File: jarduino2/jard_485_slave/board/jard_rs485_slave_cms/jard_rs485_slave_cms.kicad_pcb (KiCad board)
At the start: 2 copper layers, 94 x 94 mm, 56 parts, among them J1 NETWORK IN, J10 Conn_01x02, J2 NETWORK OUT, J3 LED, J4 Conn_01x03, J5 Conn_01x02, J6 Conn_01x03, J7 Conn_01x03, J8 Conn_01x02, J9 Conn_01x02, Q1 MMBT5550L, Q2 MMBT5550L, Q3 bpc_mos_p03p4, Q4 bpc_mos_p03p4, U1 LT1785AxN8, U2 AD8603, U3 AD8603

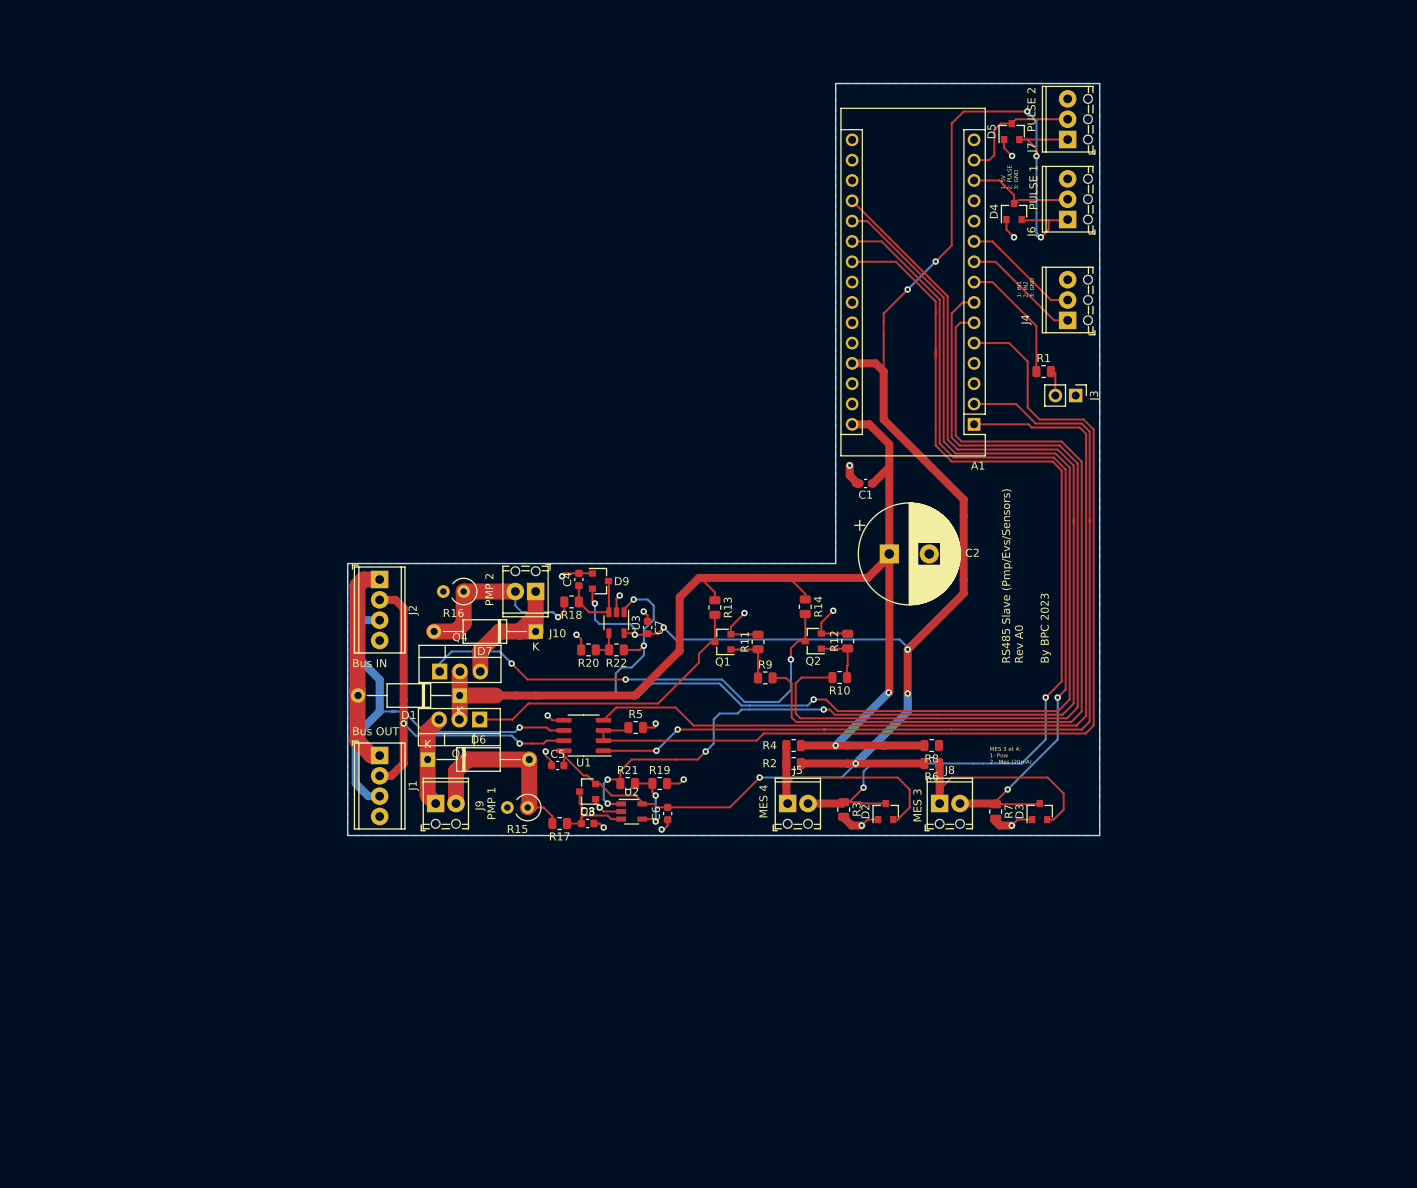
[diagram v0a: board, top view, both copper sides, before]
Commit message: Agrandir sérigraphie connecteurs bus Correction erreur inversion sérigraphie 1 et 4 sur J2 Correction inversion RX/TX sur module RS485 Inversion sérigraphie Niveaux/Débit
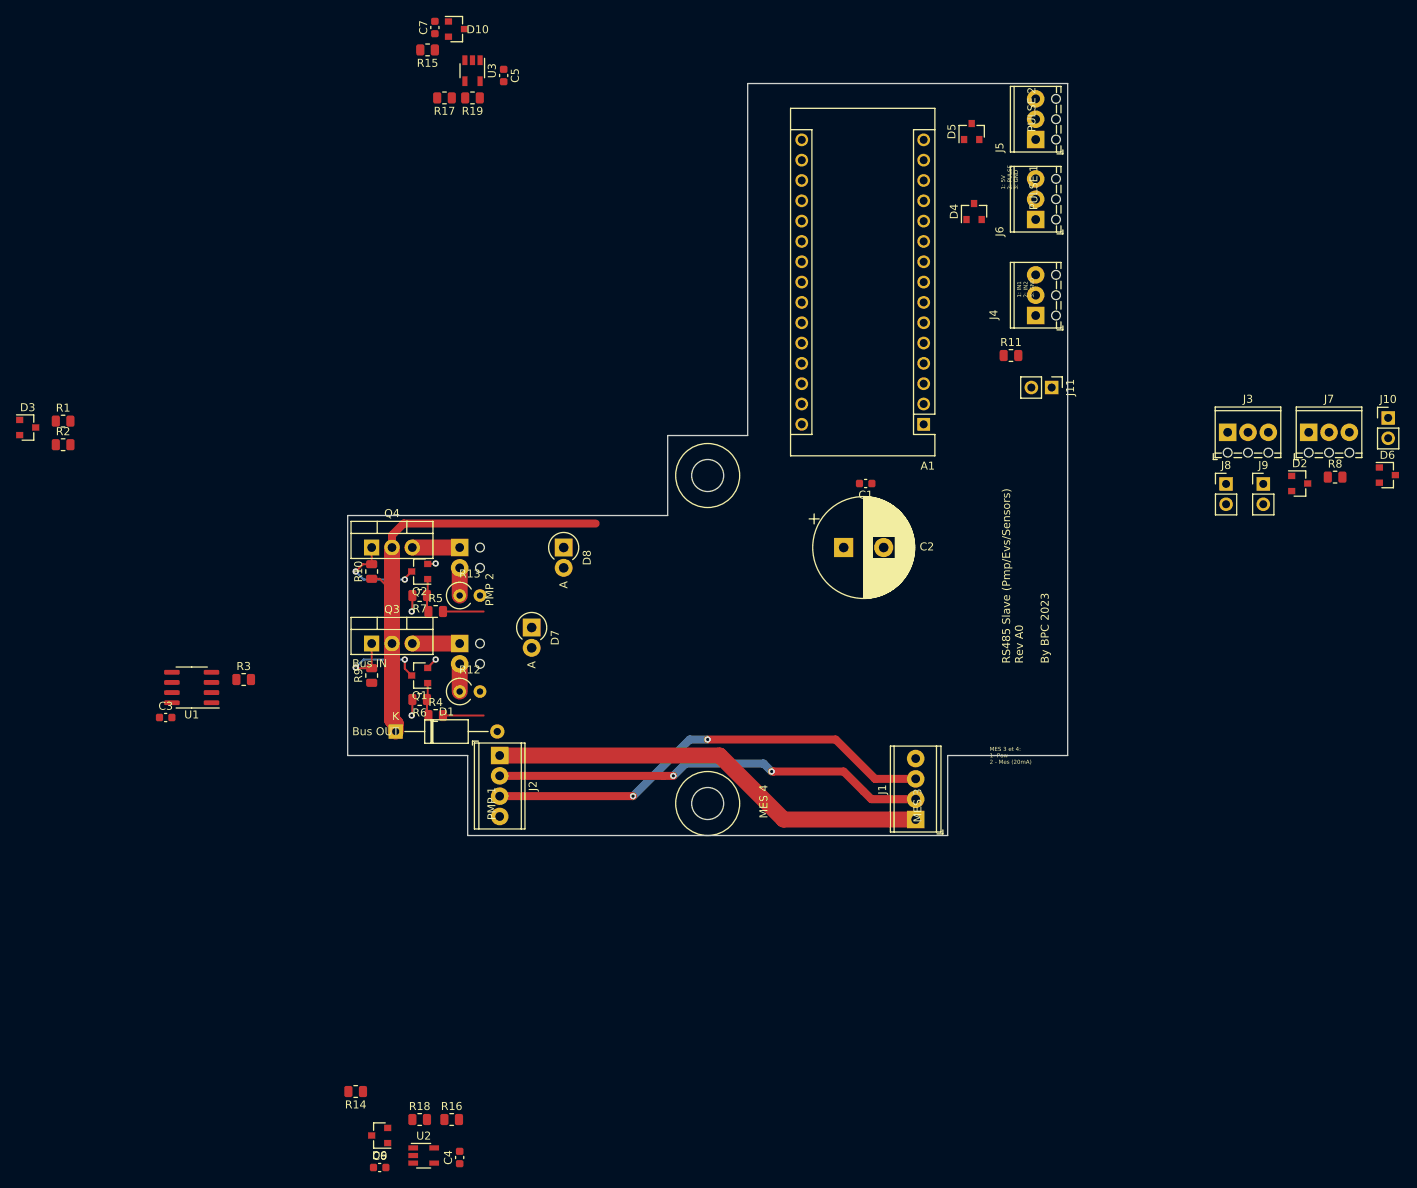
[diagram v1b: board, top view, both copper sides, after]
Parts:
- removed the D7 at (103.5, 114.5)
- removed the J5 at (135.0, 136.0)
- removed the R12 at (142.5, 115.7)
- removed the R3 at (142.0, 136.8)
- removed the R4 at (135.8, 128.8)
- removed the R6 at (153.0, 131.0)
- added D6: BAV99, Package_TO_SOT_SMD:SOT-23, F.Cu at (210.0, 95.0)
- added D8: D, Diode_THT:D_DO-15_P2.54mm_Vertical_AnodeUp, F.Cu at (107.0, 104.0)
- added J10: LED 1, Connector_PinHeader_2.54mm:PinHeader_1x02_P2.54mm_Vertical, F.Cu at (210.1, 87.8)
- added J3: Conn_01x03, TerminalBlock_Phoenix:TerminalBlock_Phoenix_MPT-0,5-3-2.54_1x03_P2.54mm_Horizontal, F.Cu at (190.0, 89.6)
- added J7: Conn_01x03, TerminalBlock_Phoenix:TerminalBlock_Phoenix_MPT-0,5-3-2.54_1x03_P2.54mm_Horizontal, F.Cu at (200.1, 89.6)
- added J9: BTN 2, Connector_PinHeader_2.54mm:PinHeader_1x02_P2.54mm_Vertical, F.Cu at (194.4, 96.0)
- added R1: 100k, Resistor_SMD:R_0805_2012Metric, F.Cu at (44.4, 88.2)
- added REF**: BPC_Trou4mm_Fixation, bpc:BPC_Trou4mm_Fixation, F.Cu at (125.0, 136.0)
- added REF**: BPC_Trou4mm_Fixation, bpc:BPC_Trou4mm_Fixation, F.Cu at (125.0, 95.0)
- D7: renamed from D6; footprint Diode_THT:D_A-405_P12.70mm_Horizontal -> Diode_THT:D_DO-15_P2.54mm_Vertical_AnodeUp
- J11: renamed from J3; value LED -> LED 2
- J12: renamed from J9; moved to B.Cu
- J13: renamed from J10; moved to B.Cu
- J8: value Conn_01x02 -> BTN 1; footprint TerminalBlock_Phoenix:TerminalBlock_Phoenix_MPT-0,5-2-2.54_1x02_P2.54mm_Horizontal -> Connector_PinHeader_2.54mm:PinHeader_1x02_P2.54mm_Vertical
- R2: value 0 -> 40k
- R7: value 250 -> 100k
- R8: value 0 -> 150
- moved D3 135.3 mm to (40.0, 89.0), turned to 0 degrees
- moved R2 99.6 mm to (44.4, 91.2)
- moved R7 76.9 mm to (89.0, 110.0), turned to 180 degrees
- moved C5 71.3 mm to (99.5, 45.0)
- moved C7 71.3 mm to (90.9, 39.0)
- moved D10 71.3 mm to (93.6, 39.2)
- moved R15 71.3 mm to (90.0, 41.8)
- moved R17 71.3 mm to (92.1, 47.8)
- moved R19 71.3 mm to (95.6, 47.8)
- moved U3 71.3 mm to (95.6, 44.4)
- moved J1 67.5 mm to (151.0, 138.0), turned to 90 degrees
- moved D2 66.0 mm to (199.0, 96.0), turned to 0 degrees
- moved R8 60.6 mm to (203.4, 95.2), turned to 0 degrees
- moved R10 54.4 mm to (83.0, 107.0), turned to 90 degrees
- moved J8 53.6 mm to (189.8, 96.0)
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- renumbered C5 to C3, C6 to C4, C7 to C5, C3 to C6, C4 to C7, D9 to D10, D8 to D9, J7 to J5, R14 to R10, R1 to R11, R15 to R12, R16 to R13, R17 to R14, R18 to R15, R19 to R16, R20 to R17, R21 to R18, R22 to R19, R5 to R3, R9 to R4, R10 to R5, R11 to R6, R13 to R9
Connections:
- A1 pad 10: IN_2 -> LED1
- A1 pad 11: Net-(A1-Pad11) -> LED2
- A1 pad 12: Net-(A1-Pad12) -> IN_1
- A1 pad 13: IN_PULSE_1 -> IN_2
- A1 pad 14: IN_PULSE_2 -> CMD_P1
- A1 pad 15: Net-(A1-Pad15) -> CMD_P2
- A1 pad 24: Net-(A1-Pad24) -> MES_POW
- A1 pad 25: Net-(A1-Pad25) -> BTN1
- A1 pad 26: Net-(A1-Pad26) -> BTN2
- A1 pad 5: TXEN -> IN_PULSE_1
- A1 pad 6: CMD_P1 -> IN_PULSE_2
- A1 pad 7: CMD_P2 -> IN_PULSE_3
- A1 pad 8: Net-(A1-Pad8) -> IN_PULSE_4
- A1 pad 9: IN_1 -> TXEN
- D2 pad 2: Net-(D2-Pad2) -> Vcc
- D2 pad 3: MESI_4 -> IN_PULSE_1
- D3 pad 2: Net-(D3-Pad2) -> Vcc
- D3 pad 3: MESI_3 -> MES_POW
- D4 pad 3: IN_PULSE_1 -> IN_PULSE_3
- D5 pad 3: IN_PULSE_2 -> IN_PULSE_4
- J5 pad 2: IN_PULSE_2 -> IN_PULSE_4
- J6 pad 2: IN_PULSE_1 -> IN_PULSE_3
- J8 pad 1: Net-(D3-Pad2) -> GND
- J8 pad 2: MESI_3 -> BTN1
- R11 pad 1: Net-(A1-Pad8) -> LED2
- R2 pad 1: Net-(D2-Pad2) -> MES_POW
- R2 pad 2: Vcc -> GND
- R7 pad 1: MESI_3 -> Net-(Q2-Pad1)
- R8 pad 1: Net-(D3-Pad2) -> LED1
- R8 pad 2: POW_MOS -> Net-(J10-Pad2)
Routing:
- net Vcc: track 248.0 -> 0.00 mm, vias 12 -> 0
- net MESI_2: track 161.1 -> 0.00 mm, vias 3 -> 0
- net MESI_1: track 153.0 -> 0.00 mm, vias 4 -> 0
- net TXEN: track 126.4 -> 0.00 mm
- net MESI_4: track 122.5 -> 0.00 mm, vias 2 -> 0
- net RX: track 114.9 -> 0.00 mm, vias 2 -> 0
- net TX: track 112.2 -> 0.00 mm
- net CMD_P2: track 111.3 -> 5.09 mm
- net MESI_3: track 104.5 -> 0.00 mm, vias 2 -> 0
- net CMD_P1: track 108.3 -> 5.09 mm
- net POW_MOS: track 143.1 -> 54.0 mm, vias 2 -> 0
- net GND: track 58.3 -> 6.56 mm, vias 18 -> 4
- net Net-(Q2-Pad3): track 59.5 -> 12.4 mm, vias 3 -> 2
- net Net-(D1-Pad2): track 26.1 -> 55.3 mm
- net Net-(D2-Pad2): track 28.7 -> 0.00 mm
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- removed copper zone on B.Cu, net GND
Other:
- board size 94 x 94 mm -> 90 x 94 mm
